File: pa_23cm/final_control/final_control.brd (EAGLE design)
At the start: 101.6 x 76.2 mm, 12 parts, among them IC1 MAX488CSA, IC2 7812T, IC3 7805T, J1 1X2-3.5MM

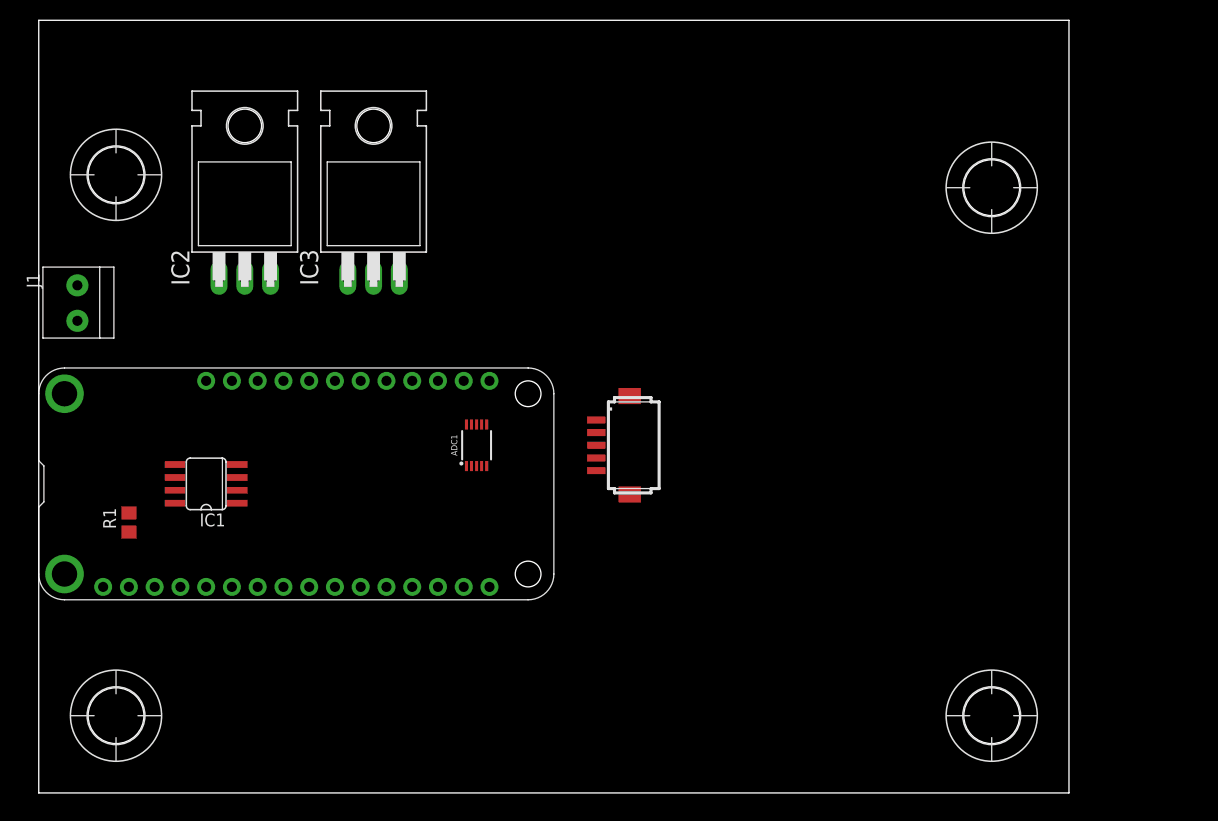
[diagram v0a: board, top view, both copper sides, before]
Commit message: aded DECOTEC enclosure parts to library.  Updates to final control board.
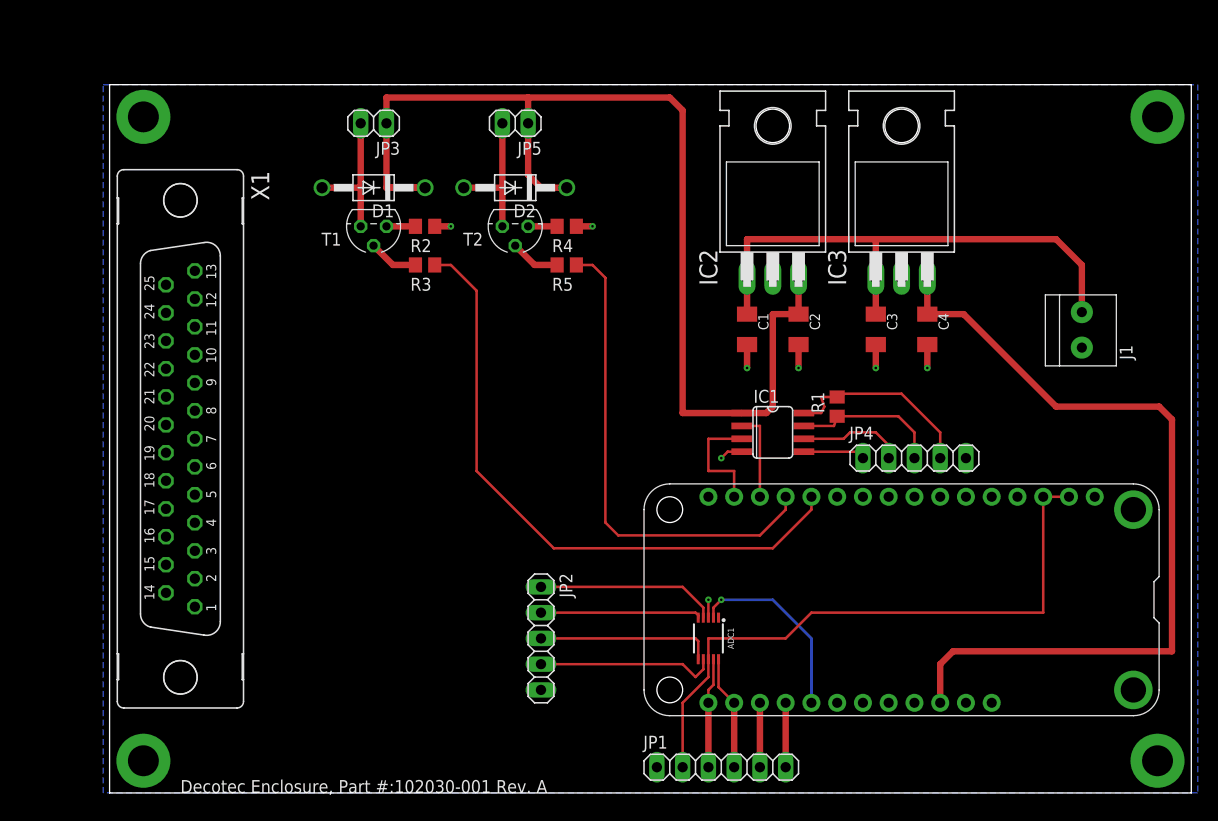
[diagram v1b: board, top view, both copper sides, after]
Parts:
- removed H1, H2, H3, H4: MOUNT-HOLE5.5, holes:5,5
- removed U$1: DF13-5P-1.25H, con-hirose-df13:DF13A-5P-1.25H
- added C1, C2, C3, C4: (no value), rcl:C1206K
- added D1, D2: 1N4004, diode:DO41-10
- added JP1: (no value), pinhead:1X06
- added JP2, JP4: (no value), pinhead:1X05
- added JP3, JP5: (no value), pinhead:1X02
- added R2, R4: 330, resistor:R0805
- added R3, R5: 1k, resistor:R0805
- added T1, T2: 2N3904, transistor:TO92
- added U$2: DECOTEC_102030-001A, vtgs:DECOTEC_102030-001A
- added X1: (no value), SparkFun-Retired:F25V
- moved FEATHER_32U4 111.1 mm to (110.5, 30.5), turned to 180 degrees
- moved J1 99.1 mm to (102.9, 45.7), turned to 270 degrees
- moved R1 70.8 mm to (78.7, 38.1)
- moved IC1 56.1 mm to (72.4, 35.6), turned to 270 degrees
- moved IC2 52.1 mm to (72.4, 61.0)
- moved IC3 52.1 mm to (85.1, 61.0)
- moved ADC1 29.8 mm to (66.0, 15.2), turned to 180 degrees
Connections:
- new net +5V: C4.1, FEATHER_32U4.26, IC3.3
- new net ADC1_ALT: ADC1.2, FEATHER_32U4.21
- new net ALERT_I: FEATHER_32U4.19, JP1.5
- new net ALERT_T: FEATHER_32U4.20, JP1.6
- new net N$10: R2.2, T1.3
- new net N$11: R3.2, T1.2
- new net N$12: X1.1
- new net N$13: X1.2
- new net N$14: X1.3
- new net N$15: X1.4
- new net N$16: X1.5
- new net PA_PTT: FEATHER_32U4.12, R3.1
- new net PA_PWR: FEATHER_32U4.13, R5.1
- new net RS485_A: IC1.8, JP4.4, R1.2
- new net RS485_B: IC1.7, JP4.3, R1.1
- new net RS485_Y: IC1.5, JP4.1
- new net RS485_Z: IC1.6, JP4.2
- new net SCL: ADC1.10, FEATHER_32U4.18, JP1.4
- new net SDA: ADC1.9, FEATHER_32U4.17, JP1.3
- new net VIN: C1.1, C3.1, IC2.1, IC3.1, J1.2
- net +12V: now also C2.1, D1.C, D2.C, IC2.3, JP3.1, JP5.1
- net +3V3: now also FEATHER_32U4.2, FEATHER_32U4.3, JP1.2
- net GND: now also C1.2, C2.2, C3.2, C4.2, IC2.2, IC3.2, JP1.1, JP2.5, JP4.5, R2.1, R4.1, U$2.PAD1, U$2.PAD2, U$2.PAD3, U$2.PAD4; no longer U$1.P$5
- net N$1: now also ADC1.1; no longer IC1.8, R1.2
- net N$2: now also D2.A, JP5.2, T2.1; no longer IC1.7, R1.1
- net N$3: now also R4.2, T2.3; no longer ADC1.10, FEATHER_32U4.18
- net N$4: now also R5.2, T2.2; no longer ADC1.9, FEATHER_32U4.17
- net N$5: now also JP2.1; no longer U$1.P$1
- net N$6: now also JP2.2; no longer U$1.P$2
- net N$7: now also JP2.3; no longer U$1.P$3
- net N$8: now also JP2.4; no longer U$1.P$4
- net N$9: now also D1.A, JP3.2, T1.1; no longer IC2.1, J1.2
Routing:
- net +12V: track 0.00 -> 112.5 mm
- net +5V: track 0.00 -> 82.1 mm
- net PA_PTT: track 0.00 -> 62.0 mm
- net +3V3: track 0.00 -> 61.8 mm
- net VIN: track 0.00 -> 53.5 mm
- net PA_PWR: track 0.00 -> 48.1 mm
- net RS485_A: track 0.00 -> 19.4 mm
- net ADC1_ALT: track 0.00 -> 18.9 mm, vias 0 -> 1
- net N$8: track 0.00 -> 17.8 mm
- net N$5: track 0.00 -> 17.8 mm
- net N$7: track 0.00 -> 17.4 mm
- net GND: track 0.00 -> 16.4 mm, vias 0 -> 8
- net N$6: track 0.00 -> 15.8 mm
- net RS485_B: track 0.00 -> 14.8 mm
- net N$2: track 0.00 -> 14.1 mm
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- added copper zone on layer 16, net GND
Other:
- board size 101.6 x 76.2 mm -> 106.7 x 69.8 mm
